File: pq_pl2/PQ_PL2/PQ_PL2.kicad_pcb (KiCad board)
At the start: 4 copper layers, 40 x 40 mm, 70 parts, among them J1 SLW-110-01-T-S, J2 SLW-110-01-T-S, J3 SLW-110-01-T-S, J4 SLW-110-01-T-S, J5 U.FL-R-SMT, J6 MS-156C3, J7 MS-156C3, J8 U.FL-R-SMT, U1 LEE2-6+, U2 MAX2121, U3 LT5537EDDB, U4 LT3048, X1 406C35B14M

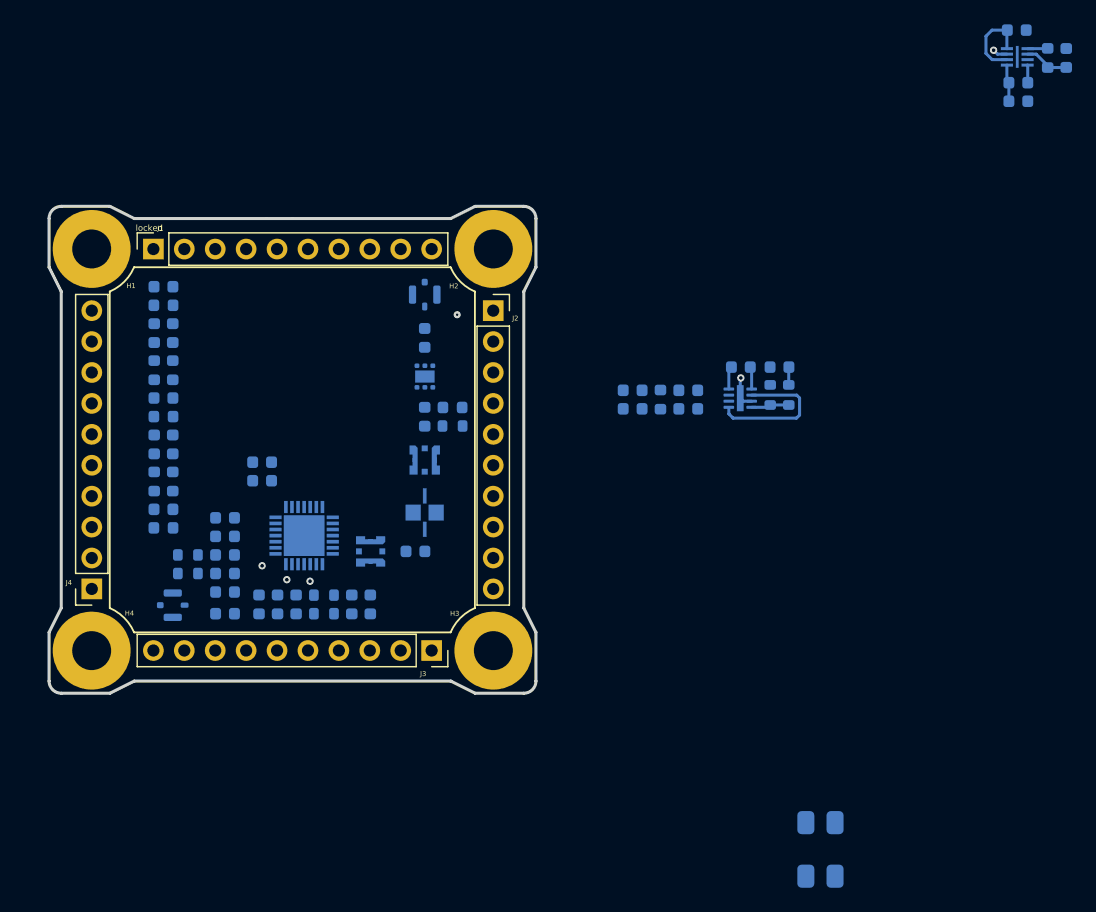
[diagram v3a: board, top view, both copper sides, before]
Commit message: Payload 2 Schematic and PCB update. Pedning final verification and manufacturing
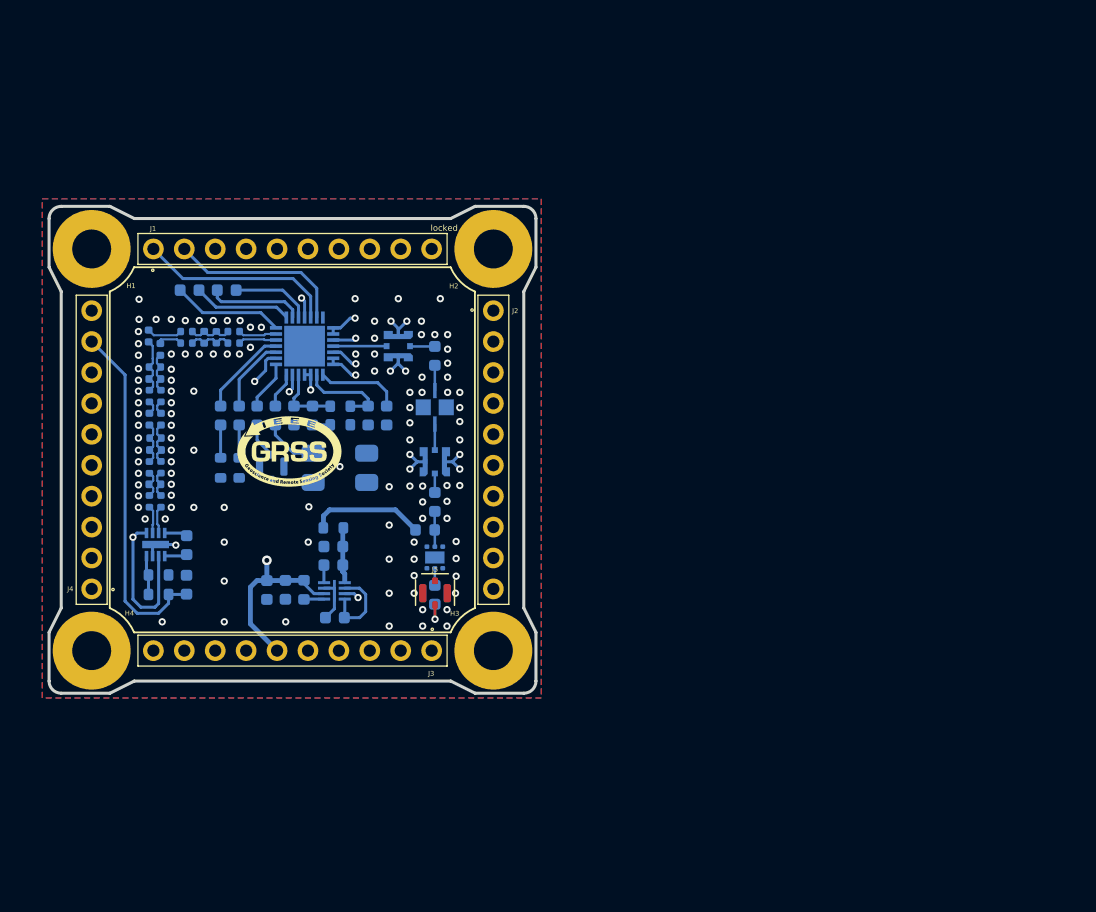
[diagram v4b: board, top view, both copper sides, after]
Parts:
- Annotation2, J5: moved to F.Cu
- C17, C18, C19, C20, C21, C22, C23, C24, C25, C26, C27, C7, C8: footprint Capacitor_SMD:C_0603_1608Metric -> Capacitor_SMD:C_0402_1005Metric
- J1, J2, J3, J4: footprint -nsl_connector:SLW-110-01 -> -nsl_connector:BBL-110-Y-X
- L2, L3, L4, L5, L6, L7, L8, L9: footprint Inductor_SMD:L_0603_1608Metric -> Inductor_SMD:L_0402_1005Metric
- U3: value LT5537EDDB -> ~; footprint Package_DFN_QFN:DFN-8-1EP_2x3mm_P0.5mm_EP0.56x2.15mm -> -nsl_rf:SON50P200X300X80-9N-D
- moved Annotation2 78.1 mm to (102.8, 59.3), turned to 0 degrees
- moved C30 77.6 mm to (102.5, 70.6), turned to -90 degrees
- moved L10 75.1 mm to (104.0, 70.6), turned to -90 degrees
- moved C31 73.9 mm to (106.5, 72.9), turned to 180 degrees
- moved Annotation1 72.8 mm to (101.0, 67.2)
- moved U4 71.2 mm to (106.5, 70.7), turned to 0 degrees
- moved C32 68.8 mm to (106.4, 68.6), turned to 0 degrees
- moved C33 67.1 mm to (106.4, 67.1), turned to 0 degrees
- moved R7 54.3 mm to (92.0, 71.0), turned to 0 degrees
- moved R6 52.4 mm to (92.0, 69.4), turned to 180 degrees
- moved C28 51.9 mm to (94.3, 70.2), turned to 90 degrees
- moved X1 50.4 mm to (107.0, 60.6), turned to 0 degrees
- moved U3 49.5 mm to (91.8, 66.9), turned to -90 degrees
- moved C29 47.8 mm to (94.4, 66.9), turned to 90 degrees
- moved C26 44.9 mm to (91.3, 63.4), turned to 90 degrees
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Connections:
- net Net-(C18-Pad1) renamed A+
- net Net-(C19-Pad1) renamed A-
- net Net-(C20-Pad1) renamed B-
- net Net-(C20-Pad2) renamed B+
- net Net-(C21-Pad1) renamed C+
- net Net-(C22-Pad1) renamed C-
- net Net-(C24-Pad1) renamed D+
- net Net-(C25-Pad1) renamed D-
- net Net-(U3-IN+) renamed E+
- net Net-(U3-IN-) renamed E-
- C24 pad 2: RSSI+ -> RSSI-
- C25 pad 2: RSSI- -> RSSI+
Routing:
- net P/L_POWER: track 17.0 -> 95.2 mm, vias 3 -> 8
- net DAC_PL: track 0.00 -> 29.7 mm, vias 0 -> 1
- net ADC_PL: track 1.47 -> 29.0 mm
- net GND: track 2.72 -> 20.6 mm, vias 2 -> 123
- net SDA1: track 0.00 -> 16.3 mm
- net SCL1: track 0.00 -> 14.6 mm
- net Net-(L1-Pad1): track 0.00 -> 9.44 mm
- net Net-(U2-IDC+): track 0.00 -> 9.16 mm
- net Net-(U2-IDC-): track 0.00 -> 8.14 mm
- net Net-(U2-QDC+): track 0.00 -> 7.88 mm
- net Net-(U2-TUNEVCO): track 0.00 -> 7.61 mm
- net Net-(U2-QOUT-): track 0.00 -> 7.36 mm
- net Net-(U2-BYPVCO): track 0.00 -> 7.00 mm
- net Net-(U2-QDC-): track 0.00 -> 6.61 mm
- net Net-(U2-QOUT+): track 0.00 -> 6.15 mm
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- added copper zone on B.Cu, net GND
- added copper zone on F.Cu, net GND
- added copper zone on In1.Cu, net GND
- added copper zone on In2.Cu, net GND

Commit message: Finished Payload 2 Schematic + PCB + BOM + Gerber + STEP Version 3.0
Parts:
- removed X1: 406C35B14M, -nsl_miscellaneous:406C35B14M
- added Annotation3: Silkscreen_Annotation, -nsl_symbols:NSL_long, F.Cu at (103.8, 47.5)
- added Annotation4: Silkscreen_Annotation, -nsl_symbols:IEEE_logo, F.Cu at (114.8, 58.8)
- added Annotation5: Silkscreen_Annotation, -nsl_symbols:UPC_positiu, F.Cu at (102.5, 70.4)
- added C34: 47nF, Capacitor_SMD:C_0603_1608Metric, B.Cu at (107.0, 61.8)
- added Y1: ECS-TXO-2016MV, -nsl_passive:ECSTXO201633320TR, B.Cu at (107.0, 59.7)
- C11: value 82pF -> 2.2pF
- C12: value 10nF -> 270pF
- C13: value 1.2nF -> 22pF
- R4: value 18k -> 120k
- R5: value 2.2k -> 15k
- moved Annotation2 11.1 mm to (91.7, 59.1), turned to -90 degrees
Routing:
- net P/L_POWER: track 95.2 -> 109.4 mm, vias 8 -> 9
- net Net-(Y1-Out): track 4.55 -> 5.98 mm
- net GND: track 20.6 -> 20.7 mm, vias 123 -> 114

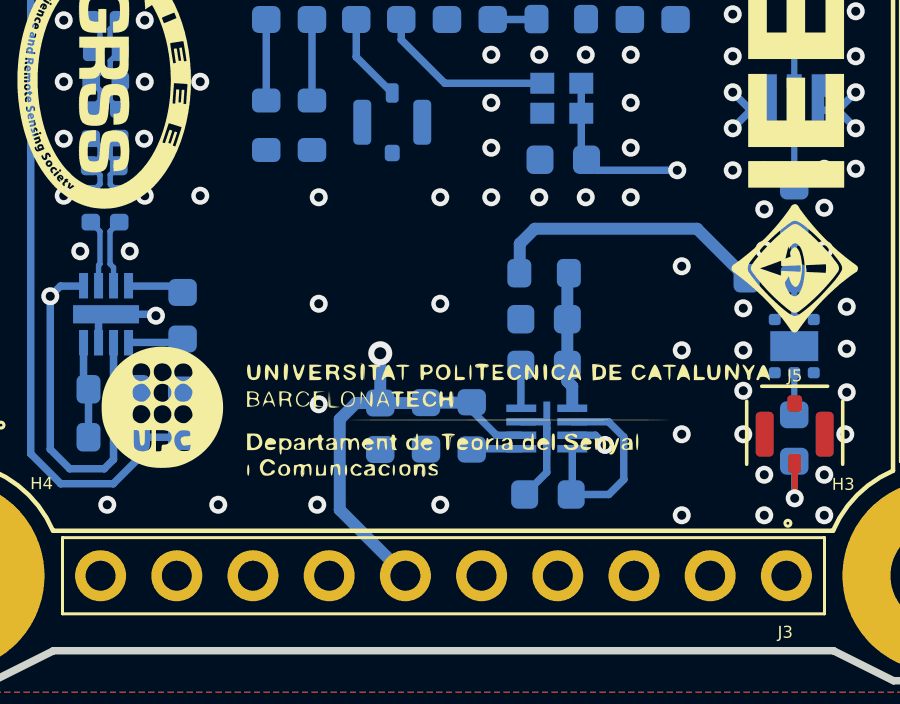
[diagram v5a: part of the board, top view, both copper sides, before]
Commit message: Payload 2 V3.1 - Added photodiode, associated Opamp and routing to pin STM PB0
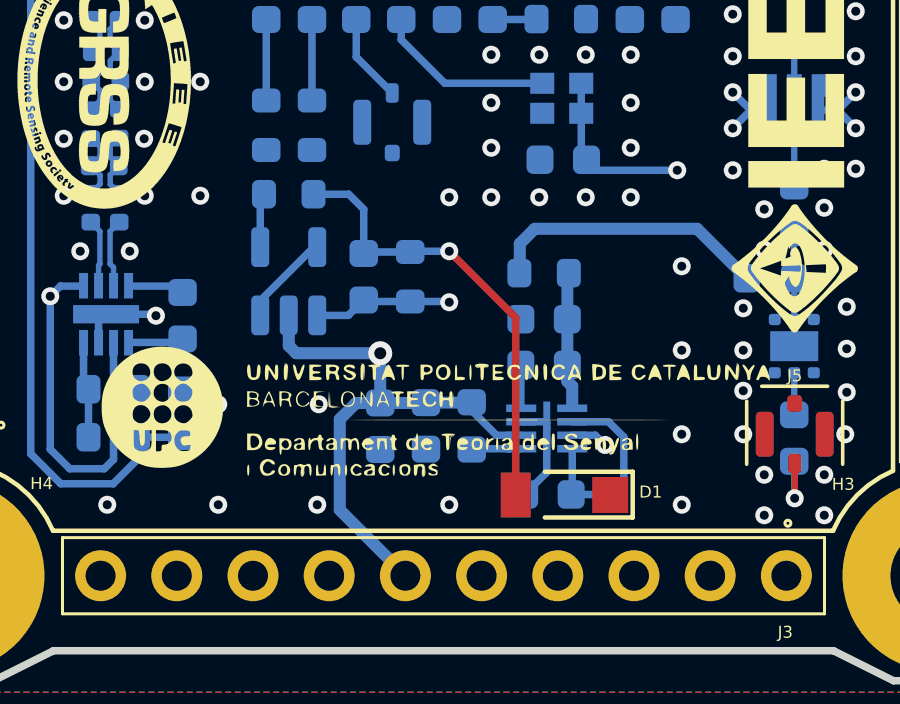
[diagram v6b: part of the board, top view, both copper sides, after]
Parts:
- added C35: 100 pF, Capacitor_SMD:C_0603_1608Metric, B.Cu at (100.4, 65.7)
- added D1: SLCD-61N8, -nsl_passive:SLCD-61N8, F.Cu at (107.3, 72.8)
- added R8: 100, Resistor_SMD:R_0603_1608Metric, B.Cu at (97.9, 62.9)
- added R9: 2k, Resistor_SMD:R_0603_1608Metric, B.Cu at (102.0, 65.7)
- added U5: LT071DBV, Package_TO_SOT_SMD:TSOT-23-5, B.Cu at (97.9, 65.8)
- J1, J2, J3, J4: value SLW-110-01-T-S -> BBL-110-Y-X
- moved Annotation1 24.0 mm to (114.2, 47.1)
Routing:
- net STM32_PB0: track 0.00 -> 20.9 mm, vias 0 -> 1
- net Net-(C35-Pad2): track 0.00 -> 15.3 mm, vias 0 -> 1
- net P/L_POWER: track 109.4 -> 116.7 mm
- net GND: track 20.7 -> 23.8 mm, vias 114 -> 112
- net Net-(U5--): track 0.00 -> 1.81 mm
